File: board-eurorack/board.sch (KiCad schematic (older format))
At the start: 64 parts, among them J1 Power, J10 B3, J12 C, J13 C1, J14 C2, J15 C3, J17 D, J18 D1, J19 D2, J2 A, J20 D3, J3 A1, J4 A2, J5 A3, J7 B, J8 B1, J9 B2, U1 OPA4197, U2 OPA4197, U4 OPA4197, U6 OPA4197

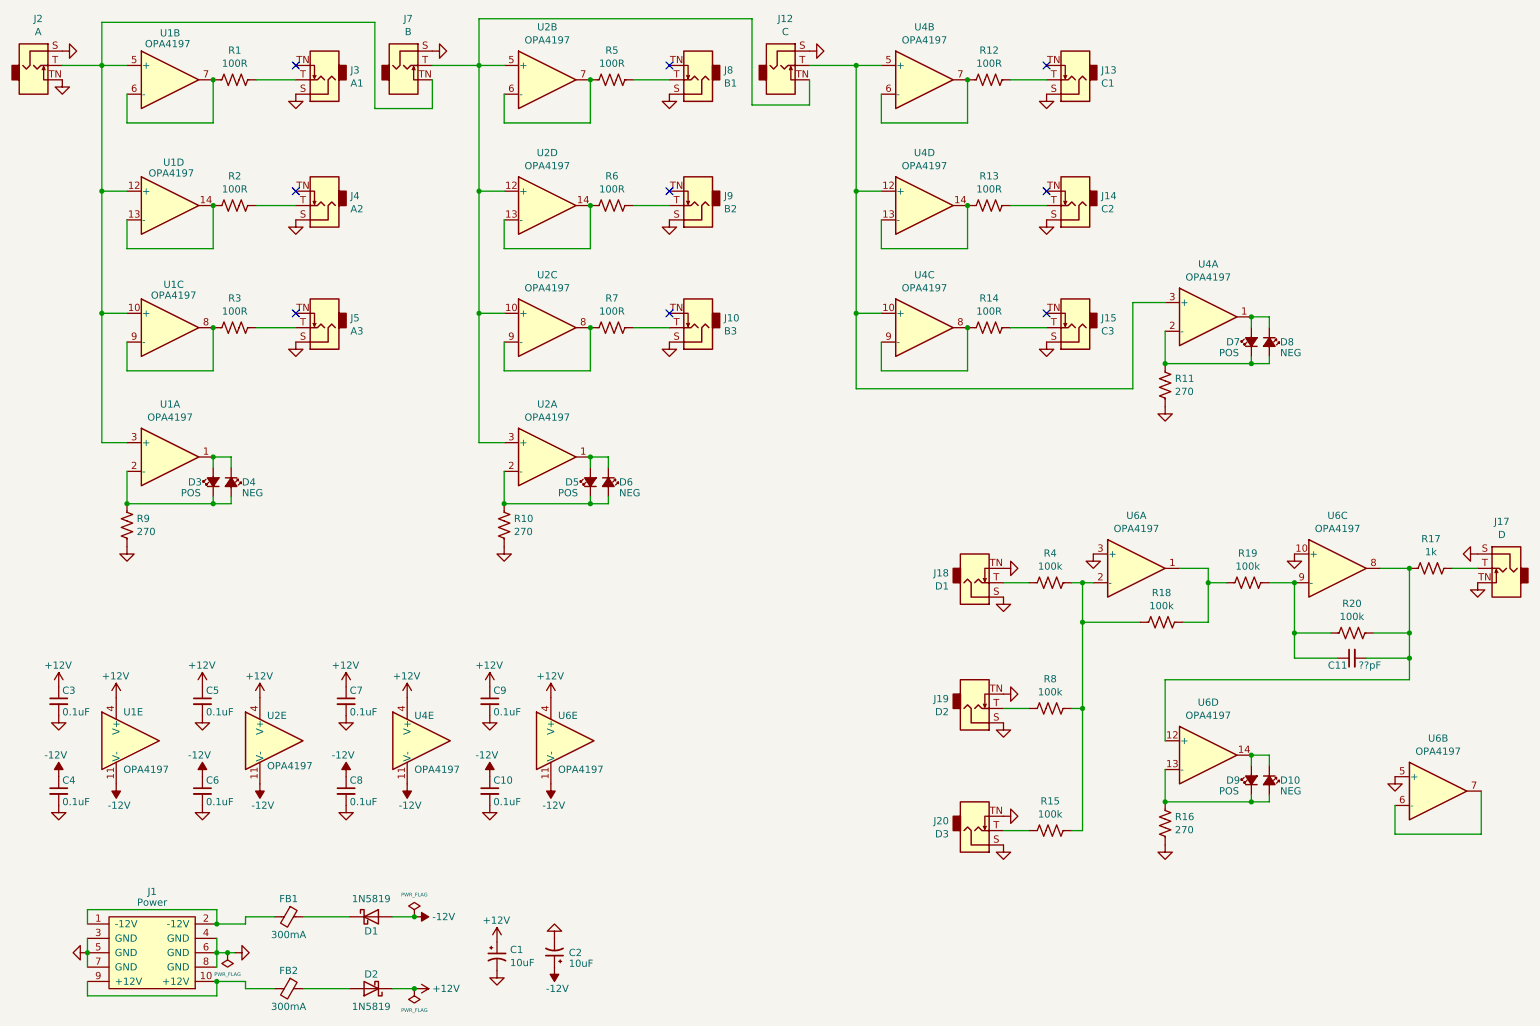
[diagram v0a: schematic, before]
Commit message: Changes from tests on first revision
1. Silkscreen legibility changes
2. Added version numbers and such to page info blocks
3. Change MPNs and values
4. Change footprints for LEDs and Diodes.
5. Pin one markers
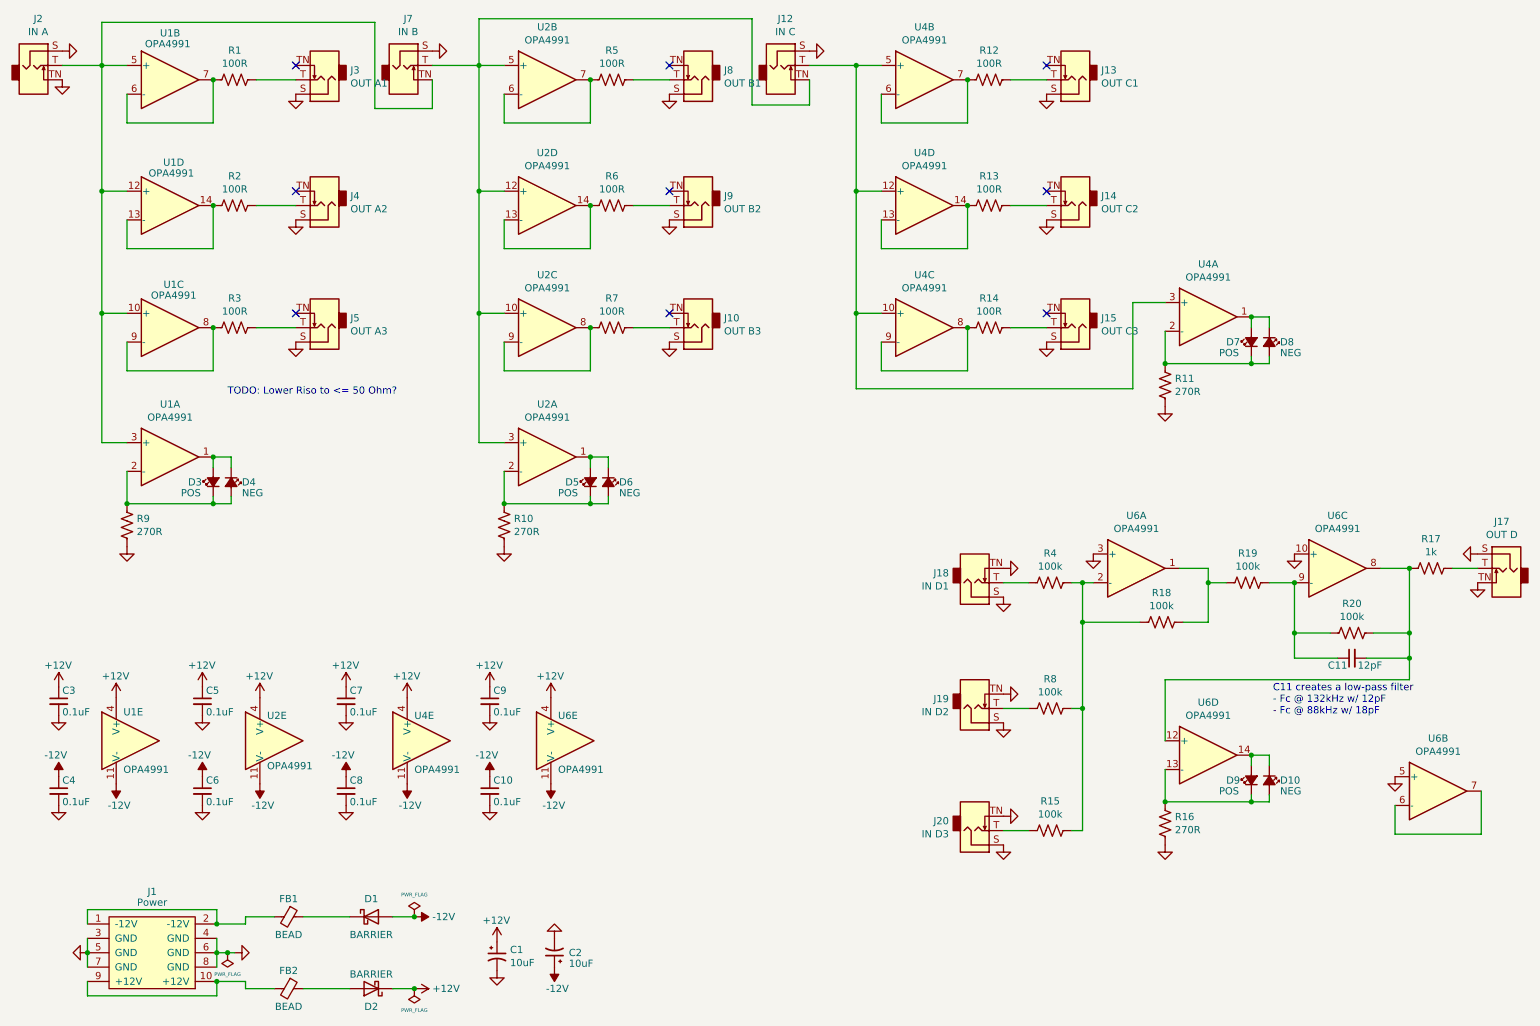
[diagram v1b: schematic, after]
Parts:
- C1, C2: Notes (none) -> 0805, 25V+, 10%, Bulk cap; unit cost 0.17 -> (none)
- C10, C3, C4, C5, C6, C7, C8, C9: Notes (none) -> 0603, 25V+, 10%, Bypass cap; unit cost 0.03 -> (none)
- C11: value ??pF -> 12pF; Notes (none) -> 0603, 25V+, 10%, Low-pass filter cap; mpn (none) -> C0603C120K5HACTU
- D1, D2: value 1N5819 -> BARRIER; footprint winterbloom:D_SOD-323_HandSoldering -> winterbloom:DIODE_SOD-123_SOD-123F; Notes (none) -> Any PMEGxxxxEGW part, 500mA If; mpn PMEG4010EGWX -> PMEG2005EGWX; unit cost 0.22 -> (none)
- D10, D4, D6, D8: footprint LED_SMD:LED_0805_2012Metric_Pad1.15x1.40mm_HandSolder -> winterbloom:LED_0805_Kingbright_APT2012; mpn 151033RS03000 -> APT2012SURCK; unit cost 0.17 -> (none)
- D3, D5, D7, D9: footprint LED_SMD:LED_0805_2012Metric_Pad1.15x1.40mm_HandSolder -> winterbloom:LED_0805_Kingbright_APT2012; mpn 151033BS03000 -> APT2012VBC/D; unit cost 0.24 -> (none)
- FB1, FB2: value 300mA -> BEAD; Notes (none) -> 300mA; unit cost 0.13 -> (none)
- J10: value B3 -> OUT B3
- J12: value C -> IN C
- J13: value C1 -> OUT C1
- J14: value C2 -> OUT C2
- J15: value C3 -> OUT C3
- J17: value D -> OUT D
- J18: value D1 -> IN D1
- J19: value D2 -> IN D2
- J2: value A -> IN A
- J20: value D3 -> IN D3
- J3: value A1 -> OUT A1
- J4: value A2 -> OUT A2
- J5: value A3 -> OUT A3
- J7: value B -> IN B
- J8: value B1 -> OUT B1
- J9: value B2 -> OUT B2
- R1, R12, R13, R14, R2, R3, R5, R6, R7: Notes (none) -> thin film; mpn (none) -> R0816P-101-D
- R10, R11, R16, R9: value 270 -> 270R; Notes (none) -> 5%, thick film; mpn ERA-3AED271V -> ERJ-3GEYJ271V; unit cost 0.06 -> (none)
- R15, R18, R19, R20, R4, R8: Notes (none) -> 0.05%, thin film; mpn MCT06030C1001FP500 -> ERA-3VRW1003V
- R17: Notes (none) -> 1%, thin film; mpn (none) -> ERA-3AED102V
- U1, U2, U4, U6: value OPA4197 -> OPA4991; mpn OPA4197IPW -> OPA4991IPWR
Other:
- note added: "C11 creates a low-pass filter\n- Fc @ 132kHz w/ 12pF\n- Fc @ 88kHz w/ 18pF"
- note added: "TODO: Lower Riso to <= 50 Ohm?"
